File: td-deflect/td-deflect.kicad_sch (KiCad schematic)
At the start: 81 parts, among them J10 Conn_01x02_Male, J11 Conn_01x02_Male, Q1 BSZ42DN25NS3GATMA1, Q10 IPD50R380CE, Q11 IPD50R380CE, Q2 G3R450MT17D, Q3 BSZ42DN25NS3GATMA1, Q4 BCP56, Q5 BCP53, Q6 BD139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

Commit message: replace S capacitors
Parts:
- C11: value 0.033uF -> 0.056uF; footprint Capacitor_SMD:C_1206_3216Metric_Pad1.42x1.75mm_HandSolder -> Capacitor_THT:C_Rect_L18.0mm_W5.0mm_P15.00mm_FKS3_FKP3; Digikey 1276-3159-1-ND -> 732-5795-ND; Voltage 200V -> 250V
- C13: value 0.015uF -> 0.056uF; footprint Capacitor_SMD:C_1206_3216Metric_Pad1.42x1.75mm_HandSolder -> Capacitor_THT:C_Rect_L18.0mm_W5.0mm_P15.00mm_FKS3_FKP3; Digikey 311-1980-1-ND -> 732-5795-ND; Voltage 200V -> 250V
- C14: value 0.033uF -> 0.12uF; footprint Capacitor_SMD:C_1206_3216Metric_Pad1.42x1.75mm_HandSolder -> Capacitor_THT:C_Rect_L18.0mm_W8.0mm_P15.00mm_FKS3_FKP3; Digikey 1276-3159-1-ND -> 732-5799-ND; Voltage 200V -> 250V
- C15: value 0.068uF -> 0.22uF; footprint Capacitor_SMD:C_1206_3216Metric_Pad1.42x1.75mm_HandSolder -> Capacitor_THT:C_Rect_L18.0mm_W6.0mm_P15.00mm_FKS3_FKP3; Digikey 311-4473-1-ND -> 732-5802-ND; Voltage 200V -> 250V
- C16: value 0.12uF -> 0.47uF; footprint Capacitor_SMD:C_1206_3216Metric_Pad1.42x1.75mm_HandSolder -> Capacitor_THT:C_Rect_L18.0mm_W8.0mm_P15.00mm_FKS3_FKP3; Digikey 399-17948-1-ND -> 732-5805-ND; Voltage 200V -> 250V
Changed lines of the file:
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@@
       (effects (font (size 1.27 1.27)) (justify left))
     )
-    (property "Value" "0.033uF" (id 1) (at 188.341 81.153 0)
-      (effects (font (size 1.27 1.27)) (justify left))
-    )
-    (property "Footprint" "Capacitor_SMD:C_1206_3216Metric_Pad1.42x1.75mm_HandSolder" (id 2) (at 186.3852 83.82 0)
+    (property "Value" "0.056uF" (id 1) (at 188.341 81.153 0)
+      (effects (font (size 1.27 1.27)) (justify left))
+    )
+    (property "Footprint" "Capacitor_THT:C_Rect_L18.0mm_W5.0mm_P15.00mm_FKS3_FKP3" (id 2) (at 186.3852 83.82 0)
       (effects (font (size 1.27 1.27)) hide)
     )
@@
       (effects (font (size 1.27 1.27)) hide)
     )
-    (property "Voltage" "200V" (id 4) (at 185.42 80.01 0)
-      (effects (font (size 1.27 1.27)) hide)
-    )
-    (property "Digikey" "1276-3159-1-ND " (id 5) (at 185.42 80.01 0)
+    (property "Voltage" "250V" (id 4) (at 185.42 80.01 0)
+      (effects (font (size 1.27 1.27)) hide)
+    )
+    (property "Digikey" "732-5795-ND" (id 5) (at 185.42 80.01 0)
       (effects (font (size 1.27 1.27)) hide)
     )
@@
       (effects (font (size 1.27 1.27)) (justify left))
     )
-    (property "Value" "0.015uF" (id 1) (at 203.581 81.153 0)
-      (effects (font (size 1.27 1.27)) (justify left))
-    )
-    (property "Footprint" "Capacitor_SMD:C_1206_3216Metric_Pad1.42x1.75mm_HandSolder" (id 2) (at 201.6252 83.82 0)
+    (property "Value" "0.056uF" (id 1) (at 203.581 81.153 0)
+      (effects (font (size 1.27 1.27)) (justify left))
+    )
+    (property "Footprint" "Capacitor_THT:C_Rect_L18.0mm_W5.0mm_P15.00mm_FKS3_FKP3" (id 2) (at 201.6252 83.82 0)
       (effects (font (size 1.27 1.27)) hide)
     )
@@
       (effects (font (size 1.27 1.27)) hide)
     )
-    (property "Voltage" "200V" (id 4) (at 200.66 80.01 0)
-      (effects (font (size 1.27 1.27)) hide)
-    )
-    (property "Digikey" "311-1980-1-ND " (id 5) (at 200.66 80.01 0)
+    (property "Voltage" "250V" (id 4) (at 200.66 80.01 0)
+      (effects (font (size 1.27 1.27)) hide)
+    )
+    (property "Digikey" "732-5795-ND" (id 5) (at 200.66 80.01 0)
       (effects (font (size 1.27 1.27)) hide)
     )
@@
       (effects (font (size 1.27 1.27)) (justify left))
     )
-    (property "Value" "0.068uF" (id 1) (at 231.521 81.153 0)
-      (effects (font (size 1.27 1.27)) (justify left))
-    )
-    (property "Footprint" "Capacitor_SMD:C_1206_3216Metric_Pad1.42x1.75mm_HandSolder" (id 2) (at 229.5652 83.82 0)
+    (property "Value" "0.22uF" (id 1) (at 231.521 81.153 0)
+      (effects (font (size 1.27 1.27)) (justify left))
+    )
+    (property "Footprint" "Capacitor_THT:C_Rect_L18.0mm_W6.0mm_P15.00mm_FKS3_FKP3" (id 2) (at 229.5652 83.82 0)
       (effects (font (size 1.27 1.27)) hide)
     )
@@
       (effects (font (size 1.27 1.27)) hide)
     )
-    (property "Voltage" "200V" (id 4) (at 228.6 80.01 0)
-      (effects (font (size 1.27 1.27)) hide)
-    )
-    (property "Digikey" "311-4473-1-ND " (id 5) (at 228.6 80.01 0)
+    (property "Voltage" "250V" (id 4) (at 228.6 80.01 0)
+      (effects (font (size 1.27 1.27)) hide)
+    )
+    (property "Digikey" "732-5802-ND" (id 5) (at 228.6 80.01 0)
       (effects (font (size 1.27 1.27)) hide)
     )
@@
       (effects (font (size 1.27 1.27)) (justify left))
     )
-    (property "Value" "0.12uF" (id 1) (at 245.491 81.153 0)
-      (effects (font (size 1.27 1.27)) (justify left))
-    )
-    (property "Footprint" "Capacitor_SMD:C_1206_3216Metric_Pad1.42x1.75mm_HandSolder" (id 2) (at 243.5352 83.82 0)
+    (property "Value" "0.47uF" (id 1) (at 245.491 81.153 0)
+      (effects (font (size 1.27 1.27)) (justify left))
+    )
+    (property "Footprint" "Capacitor_THT:C_Rect_L18.0mm_W8.0mm_P15.00mm_FKS3_FKP3" (id 2) (at 243.5352 83.82 0)
       (effects (font (size 1.27 1.27)) hide)
     )
@@
       (effects (font (size 1.27 1.27)) hide)
     )
-    (property "Voltage" "200V" (id 4) (at 242.57 80.01 0)
-      (effects (font (size 1.27 1.27)) hide)
-    )
-    (property "Digikey" "399-17948-1-ND " (id 5) (at 242.57 80.01 0)
+    (property "Voltage" "250V" (id 4) (at 242.57 80.01 0)
+      (effects (font (size 1.27 1.27)) hide)
+    )
+    (property "Digikey" "732-5805-ND" (id 5) (at 242.57 80.01 0)
       (effects (font (size 1.27 1.27)) hide)
     )
@@
       (effects (font (size 1.27 1.27)) (justify left))
     )
-    (property "Value" "0.033uF" (id 1) (at 217.551 81.153 0)
-      (effects (font (size 1.27 1.27)) (justify left))
-    )
-    (property "Footprint" "Capacitor_SMD:C_1206_3216Metric_Pad1.42x1.75mm_HandSolder" (id 2) (at 215.5952 83.82 0)
+    (property "Value" "0.12uF" (id 1) (at 217.551 81.153 0)
+      (effects (font (size 1.27 1.27)) (justify left))
+    )
+    (property "Footprint" "Capacitor_THT:C_Rect_L18.0mm_W8.0mm_P15.00mm_FKS3_FKP3" (id 2) (at 215.5952 83.82 0)
       (effects (font (size 1.27 1.27)) hide)
     )
@@
       (effects (font (size 1.27 1.27)) hide)
     )
-    (property "Voltage" "200V" (id 4) (at 214.63 80.01 0)
-      (effects (font (size 1.27 1.27)) hide)
-    )
-    (property "Digikey" "1276-3159-1-ND " (id 5) (at 214.63 80.01 0)
+    (property "Voltage" "250V" (id 4) (at 214.63 80.01 0)
+      (effects (font (size 1.27 1.27)) hide)
+    )
+    (property "Digikey" "732-5799-ND" (id 5) (at 214.63 80.01 0)
       (effects (font (size 1.27 1.27)) hide)
     )
@@
     )
     (path "/00000000-0000-0000-0000-00005c341ffa"
-      (reference "C11") (unit 1) (value "0.033uF") (footprint "Capacitor_SMD:C_1206_3216Metric_Pad1.42x1.75mm_HandSolder")
+      (reference "C11") (unit 1) (value "0.056uF") (footprint "Capacitor_THT:C_Rect_L18.0mm_W5.0mm_P15.00mm_FKS3_FKP3")
     )
     (path "/00000000-0000-0000-0000-00005da59eb0"
@@
     )
     (path "/00000000-0000-0000-0000-00005d9de736"
-      (reference "C13") (unit 1) (value "0.015uF") (footprint "Capacitor_SMD:C_1206_3216Metric_Pad1.42x1.75mm_HandSolder")
+      (reference "C13") (unit 1) (value "0.056uF") (footprint "Capacitor_THT:C_Rect_L18.0mm_W5.0mm_P15.00mm_FKS3_FKP3")
     )
     (path "/00000000-0000-0000-0000-00005da9ec35"
-      (reference "C14") (unit 1) (value "0.033uF") (footprint "Capacitor_SMD:C_1206_3216Metric_Pad1.42x1.75mm_HandSolder")
+      (reference "C14") (unit 1) (value "0.12uF") (footprint "Capacitor_THT:C_Rect_L18.0mm_W8.0mm_P15.00mm_FKS3_FKP3")
     )
     (path "/00000000-0000-0000-0000-00005d9deb6f"
-      (reference "C15") (unit 1) (value "0.068uF") (footprint "Capacitor_SMD:C_1206_3216Metric_Pad1.42x1.75mm_HandSolder")
+      (reference "C15") (unit 1) (value "0.22uF") (footprint "Capacitor_THT:C_Rect_L18.0mm_W6.0mm_P15.00mm_FKS3_FKP3")
     )
     (path "/00000000-0000-0000-0000-00005d9e57d3"
-      (reference "C16") (unit 1) (value "0.12uF") (footprint "Capacitor_SMD:C_1206_3216Metric_Pad1.42x1.75mm_HandSolder")
+      (reference "C16") (unit 1) (value "0.47uF") (footprint "Capacitor_THT:C_Rect_L18.0mm_W8.0mm_P15.00mm_FKS3_FKP3")
     )
     (path "/00000000-0000-0000-0000-00005c37bef7/00000000-0000-0000-0000-00005c39edb0"

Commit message: remove recirculating schottky diode
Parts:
- removed D2: C3D10170H, Package_TO_SOT_THT:TO-247-2_Vertical, symbol Diode:C3D10170H
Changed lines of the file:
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@@
   (junction (at 128.27 129.54) (diameter 0) (color 0 0 0 0)
   )
-  (junction (at 106.68 76.2) (diameter 1.016) (color 0 0 0 0)
-  )
   (junction (at 248.92 93.98) (diameter 0) (color 0 0 0 0)
   )
@@
     (stroke (width 0) (type solid) (color 0 0 0 0))
   )
-  (wire (pts (xy 97.79 76.2) (xy 106.68 76.2))
-    (stroke (width 0) (type solid) (color 0 0 0 0))
-  )
   (wire (pts (xy 130.81 76.2) (xy 163.83 76.2))
     (stroke (width 0) (type solid) (color 0 0 0 0))
@@
     (stroke (width 0) (type solid) (color 0 0 0 0))
   )
-  (wire (pts (xy 106.68 76.2) (xy 115.57 76.2))
+  (wire (pts (xy 97.79 76.2) (xy 115.57 76.2))
     (stroke (width 0) (type solid) (color 0 0 0 0))
   )
@@
     (pin "2")
   )
-  (symbol (lib_id "Diode:C3D10170H") (at 106.68 80.01 270) (unit 1)
-    (in_bom yes) (on_board yes)
-    (property "Reference" "D2" (id 0) (at 108.6866 78.8416 90)
-      (effects (font (size 1.27 1.27)) (justify left))
-    )
-    (property "Value" "C3D10170H" (id 1) (at 101.6 91.44 90)
-      (effects (font (size 1.27 1.27)) (justify left))
-    )
-    (property "Footprint" "Package_TO_SOT_THT:TO-247-2_Vertical" (id 2) (at 102.235 80.01 0)
-      (effects (font (size 1.27 1.27)) hide)
-    )
-    (property "Datasheet" "https://www.wolfspeed.com/media/downloads/96/C3D10170H.pdf" (id 3) (at 106.68 80.01 0)
-      (effects (font (size 1.27 1.27)) hide)
-    )
-    (property "Digikey" "C3D10170H-ND " (id 4) (at 106.68 80.01 0)
-      (effects (font (size 1.27 1.27)) hide)
-    )
-    (pin "1")
-    (pin "2")
-  )
-  (symbol (lib_id "power:GND") (at 106.68 83.82 0) (unit 1)
-    (in_bom yes) (on_board yes)
-    (property "Reference" "#PWR0162" (id 0) (at 106.68 90.17 0)
-      (effects (font (size 1.27 1.27)) hide)
-    )
-    (property "Value" "GND" (id 1) (at 106.807 88.2142 0))
-    (property "Footprint" "" (id 2) (at 106.68 83.82 0)
-      (effects (font (size 1.27 1.27)) hide)
-    )
-    (property "Datasheet" "" (id 3) (at 106.68 83.82 0)
-      (effects (font (size 1.27 1.27)) hide)
-    )
-    (pin "1")
-  )
   (symbol (lib_id "Connector:Conn_01x02_Male") (at 128.27 71.12 90) (mirror x) (unit 1)
     (in_bom yes) (on_board yes)
@@
       (reference "#PWR0161") (unit 1) (value "+48V") (footprint "")
     )
-    (path "/00000000-0000-0000-0000-00005daabaec"
-      (reference "#PWR0162") (unit 1) (value "GND") (footprint "")
-    )
     (path "/00000000-0000-0000-0000-00005c37bef7/00000000-0000-0000-0000-00005c3a0a6f"
       (reference "#PWR0163") (unit 1) (value "+5V") (footprint "")
@@
       (reference "D1") (unit 1) (value "ES1G-13-F") (footprint "Diode_SMD:D_SMA")
     )
-    (path "/00000000-0000-0000-0000-00005daaaa09"
-      (reference "D2") (unit 1) (value "C3D10170H") (footprint "Package_TO_SOT_THT:TO-247-2_Vertical")
-    )
     (path "/00000000-0000-0000-0000-00005d9d9196/00000000-0000-0000-0000-00005d9ef938"

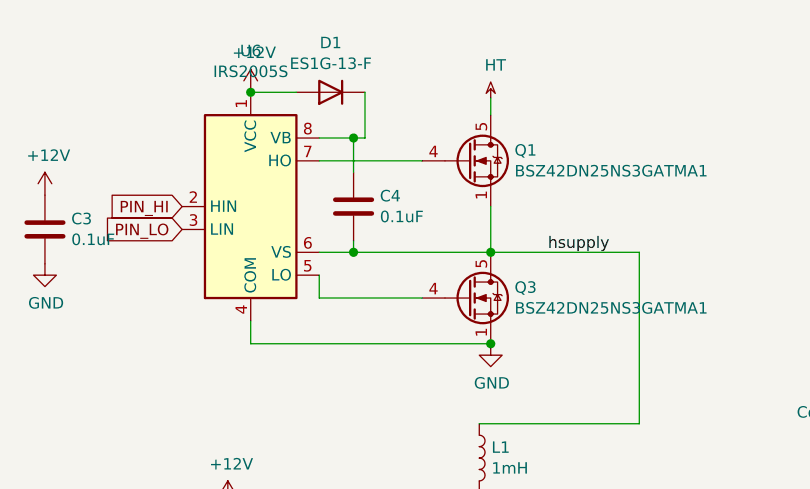
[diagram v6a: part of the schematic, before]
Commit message: add gate resistors to top drive
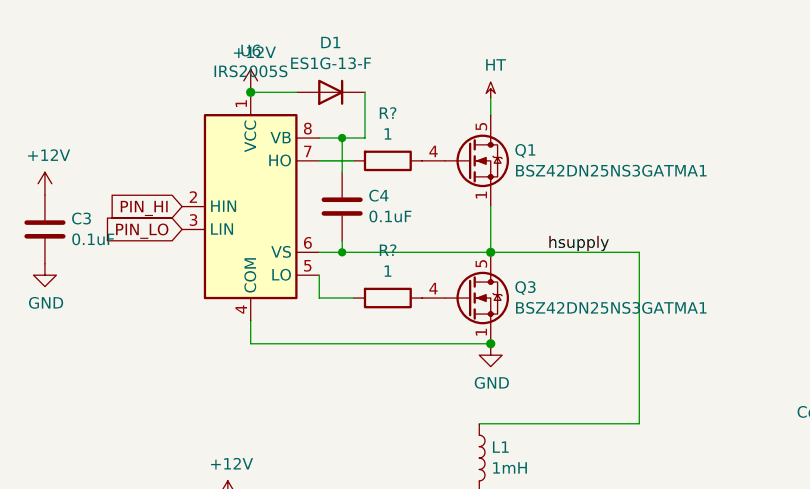
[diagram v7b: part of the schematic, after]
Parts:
- added R? (x2): 1, Resistor_SMD:R_0805_2012Metric_Pad1.15x1.40mm_HandSolder, symbol Device:R
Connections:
- net at U6.5 (LO): now also R?.2; no longer Q3.4 (G)
- net at U6.7 (HO): now also R?.2; no longer Q1.4 (G)
- new net: Q1.4 (G), R?.1
- new net: Q3.4 (G), R?.1
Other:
- moved on the sheet: C4
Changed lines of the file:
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@@
   (junction (at 259.08 25.4) (diameter 1.016) (color 0 0 0 0)
   )
+  (junction (at 71.12 33.02) (diameter 0) (color 0 0 0 0)
+  )
   (junction (at 128.27 129.54) (diameter 0) (color 0 0 0 0)
   )
@@
   (junction (at 242.57 83.82) (diameter 1.016) (color 0 0 0 0)
   )
-  (junction (at 72.39 45.72) (diameter 1.016) (color 0 0 0 0)
-  )
   (junction (at 146.05 147.32) (diameter 0) (color 0 0 0 0)
   )
@@
   (junction (at 128.27 162.56) (diameter 0) (color 0 0 0 0)
   )
-  (junction (at 72.39 33.02) (diameter 1.016) (color 0 0 0 0)
-  )
   (junction (at 146.05 154.94) (diameter 1.016) (color 0 0 0 0)
   )
@@
   (junction (at 214.63 93.98) (diameter 1.016) (color 0 0 0 0)
   )
+  (junction (at 71.12 45.72) (diameter 0) (color 0 0 0 0)
+  )
   (junction (at 124.46 76.2) (diameter 1.016) (color 0 0 0 0)
   )
@@
     (stroke (width 0) (type solid) (color 0 0 0 0))
   )
+  (wire (pts (xy 68.58 35.56) (xy 72.39 35.56))
+    (stroke (width 0) (type default) (color 0 0 0 0))
+  )
   (wire (pts (xy 87.63 30.48) (xy 87.63 28.575))
     (stroke (width 0) (type solid) (color 0 0 0 0))
@@
     (stroke (width 0) (type default) (color 0 0 0 0))
   )
+  (wire (pts (xy 68.58 50.8) (xy 72.39 50.8))
+    (stroke (width 0) (type default) (color 0 0 0 0))
+  )
   (wire (pts (xy 170.18 157.48) (xy 168.91 157.48))
     (stroke (width 0) (type solid) (color 0 0 0 0))
@@
     (stroke (width 0) (type solid) (color 0 0 0 0))
   )
-  (wire (pts (xy 72.39 45.72) (xy 87.63 45.72))
-    (stroke (width 0) (type solid) (color 0 0 0 0))
-  )
   (wire (pts (xy 138.43 180.34) (xy 142.24 180.34))
     (stroke (width 0) (type solid) (color 0 0 0 0))
@@
     (stroke (width 0) (type solid) (color 0 0 0 0))
   )
-  (wire (pts (xy 68.58 45.72) (xy 72.39 45.72))
+  (wire (pts (xy 68.58 45.72) (xy 71.12 45.72))
     (stroke (width 0) (type solid) (color 0 0 0 0))
   )
@@
     (stroke (width 0) (type default) (color 0 0 0 0))
   )
+  (wire (pts (xy 71.12 33.02) (xy 68.58 33.02))
+    (stroke (width 0) (type solid) (color 0 0 0 0))
+  )
   (wire (pts (xy 232.41 93.98) (xy 232.41 92.71))
     (stroke (width 0) (type solid) (color 0 0 0 0))
@@
     (stroke (width 0) (type solid) (color 0 0 0 0))
   )
-  (wire (pts (xy 68.58 50.8) (xy 80.01 50.8))
-    (stroke (width 0) (type solid) (color 0 0 0 0))
-  )
   (wire (pts (xy 204.47 83.82) (xy 204.47 85.09))
     (stroke (width 0) (type solid) (color 0 0 0 0))
@@
     (stroke (width 0) (type solid) (color 0 0 0 0))
   )
-  (wire (pts (xy 72.39 45.72) (xy 72.39 44.45))
-    (stroke (width 0) (type solid) (color 0 0 0 0))
-  )
   (wire (pts (xy 246.38 83.82) (xy 246.38 85.09))
     (stroke (width 0) (type solid) (color 0 0 0 0))
@@
     (stroke (width 0) (type solid) (color 0 0 0 0))
   )
-  (wire (pts (xy 68.58 35.56) (xy 80.01 35.56))
-    (stroke (width 0) (type solid) (color 0 0 0 0))
-  )
   (wire (pts (xy 104.14 64.77) (xy 104.14 45.72))
     (stroke (width 0) (type solid) (color 0 0 0 0))
@@
     (stroke (width 0) (type solid) (color 0 0 0 0))
   )
+  (wire (pts (xy 71.12 45.72) (xy 87.63 45.72))
+    (stroke (width 0) (type solid) (color 0 0 0 0))
+  )
   (wire (pts (xy 17.78 153.67) (xy 25.4 153.67))
     (stroke (width 0) (type solid) (color 0 0 0 0))
@@
     (stroke (width 0) (type solid) (color 0 0 0 0))
   )
-  (wire (pts (xy 72.39 33.02) (xy 73.66 33.02))
+  (wire (pts (xy 71.12 33.02) (xy 71.12 36.83))
+    (stroke (width 0) (type default) (color 0 0 0 0))
+  )
+  (wire (pts (xy 71.12 33.02) (xy 73.66 33.02))
     (stroke (width 0) (type solid) (color 0 0 0 0))
   )
@@
     (stroke (width 0) (type default) (color 0 0 0 0))
   )
-  (wire (pts (xy 72.39 33.02) (xy 72.39 36.83))
-    (stroke (width 0) (type solid) (color 0 0 0 0))
-  )
   (wire (pts (xy 242.57 76.2) (xy 260.35 76.2))
     (stroke (width 0) (type solid) (color 0 0 0 0))
@@
     (stroke (width 0) (type default) (color 0 0 0 0))
   )
-  (wire (pts (xy 72.39 33.02) (xy 68.58 33.02))
-    (stroke (width 0) (type solid) (color 0 0 0 0))
-  )
   (wire (pts (xy 48.26 81.28) (xy 50.8 81.28))
     (stroke (width 0) (type solid) (color 0 0 0 0))
@@
     (stroke (width 0) (type default) (color 0 0 0 0))
   )
+  (wire (pts (xy 71.12 44.45) (xy 71.12 45.72))
+    (stroke (width 0) (type default) (color 0 0 0 0))
+  )
   (wire (pts (xy 186.69 92.71) (xy 186.69 111.76))
     (stroke (width 0) (type solid) (color 0 0 0 0))
@@
     (pin "2")
   )
-  (symbol (lib_id "Device:C") (at 72.39 40.64 0) (unit 1)
+  (symbol (lib_id "Device:C") (at 71.12 40.64 0) (unit 1)
     (in_bom yes) (on_board yes)
-    (property "Reference" "C4" (id 0) (at 75.311 39.4716 0)
+    (property "Reference" "C4" (id 0) (at 74.041 39.4716 0)
       (effects (font (size 1.27 1.27)) (justify left))
     )
-    (property "Value" "0.1uF" (id 1) (at 75.311 41.783 0)
+    (property "Value" "0.1uF" (id 1) (at 74.041 41.783 0)
       (effects (font (size 1.27 1.27)) (justify left))
     )
-    (property "Footprint" "Capacitor_SMD:C_0805_2012Metric_Pad1.15x1.40mm_HandSolder" (id 2) (at 73.3552 44.45 0)
+    (property "Footprint" "Capacitor_SMD:C_0805_2012Metric_Pad1.15x1.40mm_HandSolder" (id 2) (at 72.0852 44.45 0)
       (effects (font (size 1.27 1.27)) hide)
     )
-    (property "Datasheet" "~" (id 3) (at 72.39 40.64 0)
+    (property "Datasheet" "~" (id 3) (at 71.12 40.64 0)
       (effects (font (size 1.27 1.27)) hide)
     )
-    (property "Digikey" "1276-1099-1-ND" (id 4) (at 72.39 40.64 0)
+    (property "Digikey" "1276-1099-1-ND" (id 4) (at 71.12 40.64 0)
       (effects (font (size 1.27 1.27)) hide)
     )
@@
     (pin "2")
   )
+  (symbol (lib_id "Device:R") (at 76.2 35.56 270) (unit 1)
+    (in_bom yes) (on_board yes)
+    (property "Reference" "R?" (id 0) (at 76.2 30.3022 90))
+    (property "Value" "1" (id 1) (at 76.2 32.6136 90))
+    (property "Footprint" "Resistor_SMD:R_0805_2012Metric_Pad1.15x1.40mm_HandSolder" (id 2) (at 76.2 33.782 90)
+      (effects (font (size 1.27 1.27)) hide)
+    )
+    (property "Datasheet" "~" (id 3) (at 76.2 35.56 0)
+      (effects (font (size 1.27 1.27)) hide)
+    )
+    (property "Digikey" " 311-1.00CRCT-ND" (id 4) (at 76.2 35.56 0)
+      (effects (font (size 1.27 1.27)) hide)
+    )
+    (pin "1")
+    (pin "2")
+  )
   (symbol (lib_id "Device:R") (at 241.3 97.79 0) (unit 1)
     (in_bom yes) (on_board yes)
@@
     (pin "1")
   )
+  (symbol (lib_id "Device:R") (at 76.2 50.8 270) (unit 1)
+    (in_bom yes) (on_board yes)
+    (property "Reference" "R?" (id 0) (at 76.2 45.5422 90))
+    (property "Value" "1" (id 1) (at 76.2 47.8536 90))
+    (property "Footprint" "Resistor_SMD:R_0805_2012Metric_Pad1.15x1.40mm_HandSolder" (id 2) (at 76.2 49.022 90)
+      (effects (font (size 1.27 1.27)) hide)
+    )
+    (property "Datasheet" "~" (id 3) (at 76.2 50.8 0)
+      (effects (font (size 1.27 1.27)) hide)
+    )
+    (property "Digikey" " 311-1.00CRCT-ND" (id 4) (at 76.2 50.8 0)
+      (effects (font (size 1.27 1.27)) hide)
+    )
+    (pin "1")
+    (pin "2")
+  )
   (symbol (lib_id "Device:R") (at 128.27 176.53 0) (unit 1)
     (in_bom yes) (on_board yes) (fields_autoplaced)
@@
       (reference "R?") (unit 1) (value "10") (footprint "")
     )
+    (path "/956604f0-4169-43b1-9fb2-4fdc32823a3c"
+      (reference "R?") (unit 1) (value "1") (footprint "Resistor_SMD:R_0805_2012Metric_Pad1.15x1.40mm_HandSolder")
+    )
     (path "/99288055-aaed-4c6d-853a-de42aee00748"
       (reference "R?") (unit 1) (value "1") (footprint "Resistor_SMD:R_0805_2012Metric_Pad1.15x1.40mm_HandSolder")
     )
+    (path "/d2f47dbb-e9f9-436d-8005-99f258fc996d"
+      (reference "R?") (unit 1) (value "1") (footprint "Resistor_SMD:R_0805_2012Metric_Pad1.15x1.40mm_HandSolder")
+    )
